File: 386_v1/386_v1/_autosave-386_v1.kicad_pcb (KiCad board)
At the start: 2 copper layers, 69 x 84 mm, 39 parts, among them U1 74LVC1G17GW, U10 SN74LVC4245A, U11 SN74LVC4245A, U2 74LVC1G17GW, U3 i386SX, U4 SN74LVC4245A, U5 SN74LVC4245A, U6 SN74LVC4245A, U7 Conn_02x32_Odd_Even, U8 Conn_02x32_Odd_Even, U9 SN74LVC4245A

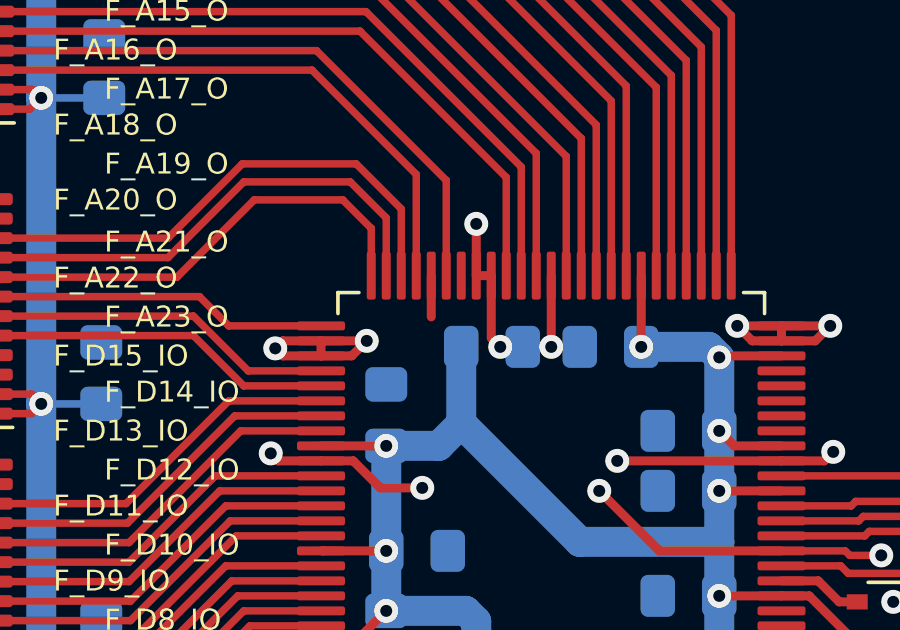
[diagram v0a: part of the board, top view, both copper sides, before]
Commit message: update schematic, use active level shifters
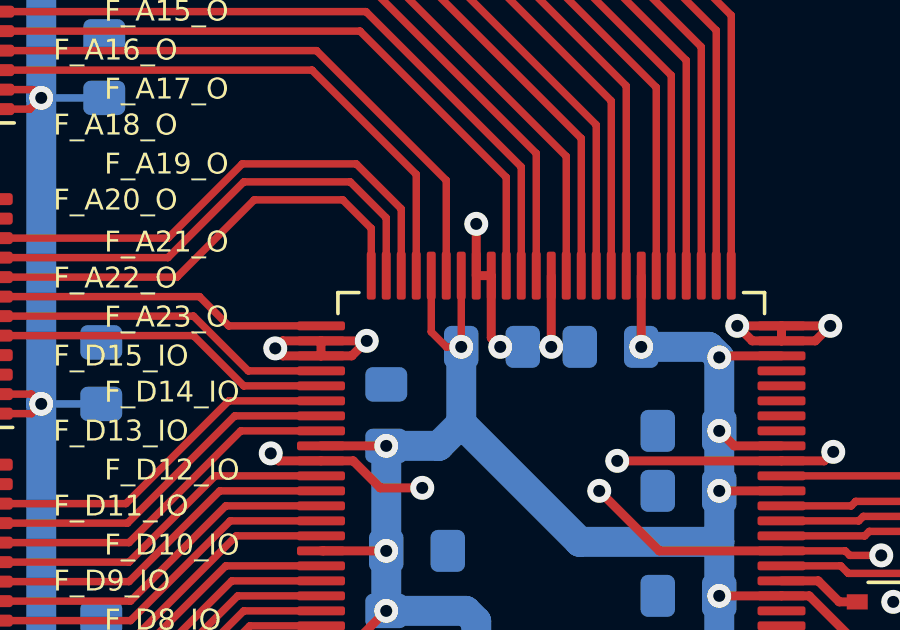
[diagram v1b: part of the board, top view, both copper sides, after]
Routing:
- net +5V: track 285.1 -> 289.2 mm, vias 16 -> 17
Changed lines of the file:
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@@
     (thickness 1.6)
     (drawings 75)
-    (tracks 722)
+    (tracks 726)
     (zones 0)
     (modules 39)
@@
   (via (at 69.2 70.3) (size 0.8) (drill 0.4) (layers F.Cu B.Cu) (net 1) (status 30))
   (segment (start 71.275 70.3) (end 69.2 70.3) (width 0.3) (layer F.Cu) (net 1) (status 10))
-  (segment (start 59.6 59.625) (end 59.6 61) (width 0.3) (layer F.Cu) (net 1) (status 10))
   (segment (start 71.3 80.3) (end 67.6 80.3) (width 1) (layer B.Cu) (net 1) (status 10))
   (segment (start 67.6 72.7) (end 67.6 80.3) (width 1) (layer B.Cu) (net 1) (status 10))
@@
   (segment (start 46.6 82) (end 48.5 82) (width 0.25) (layer B.Cu) (net 1))
   (segment (start 46.6 95.7) (end 48.4 95.7) (width 0.25) (layer B.Cu) (net 1))
+  (via (at 60.6 62) (size 0.8) (drill 0.4) (layers F.Cu B.Cu) (net 1))
+  (segment (start 60.6 59.625) (end 60.6 62) (width 0.25) (layer F.Cu) (net 1))
+  (segment (start 59.6 59.625) (end 59.6 61.5) (width 0.25) (layer F.Cu) (net 1))
+  (segment (start 60.1 62) (end 60.6 62) (width 0.25) (layer F.Cu) (net 1))
+  (segment (start 59.6 61.5) (end 60.1 62) (width 0.25) (layer F.Cu) (net 1))
   (segment (start 39.2375 92.125) (end 35.975 92.125) (width 0.25) (layer F.Cu) (net 5) (status 10))
   (segment (start 35.975 92.125) (end 35.35 92.75) (width 0.25) (layer F.Cu) (net 5))
